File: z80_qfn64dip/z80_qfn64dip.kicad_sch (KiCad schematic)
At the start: 58 parts, among them J1 Conn_08, U1 Caravel_QFN, U2 Z80CPU, U3 TPS7A2033PDQNRM3, U4 TPS7A2018PDQNRM3, U5 TPS7A2050PDQNRM3, U6 AT25EU0081A, X1 10MHz

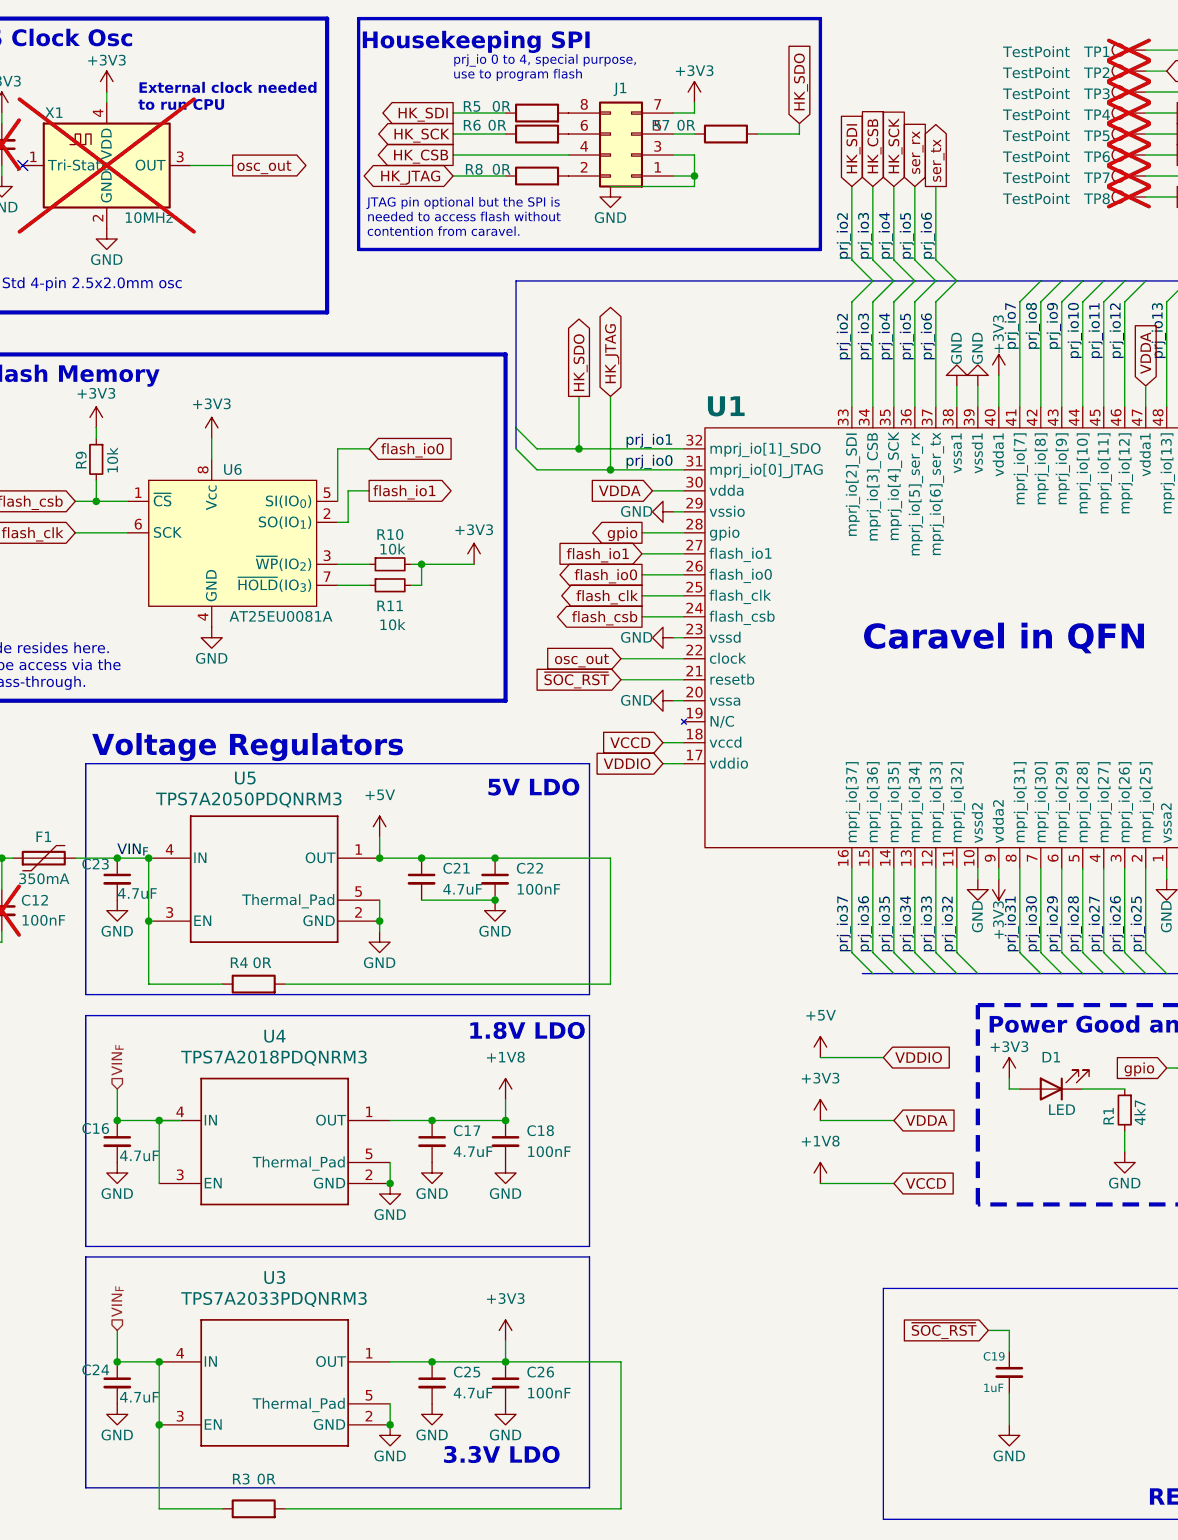
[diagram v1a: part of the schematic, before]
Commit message: remove signals from power layer moving them to bottom layer; change power routing from tracks to planes if they can be called as such
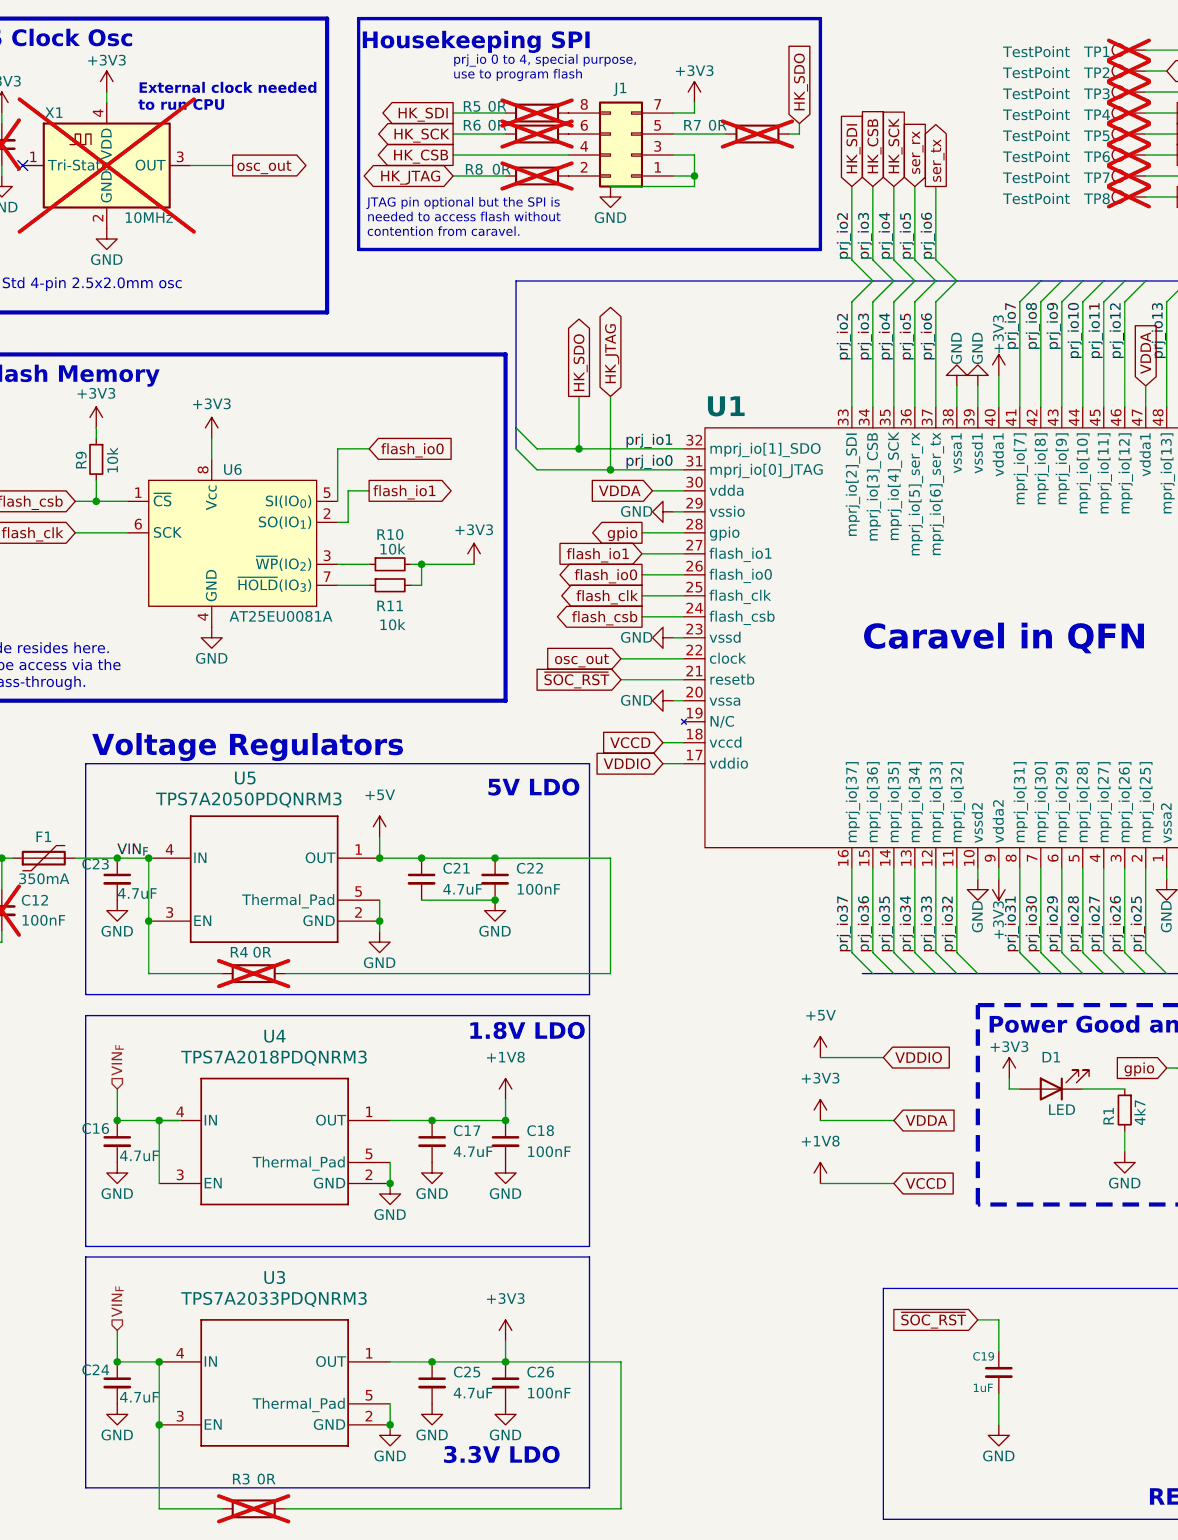
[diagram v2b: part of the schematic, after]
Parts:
- R3, R4, R5, R6, R7, R8: now not fitted
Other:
- moved on the sheet: C19
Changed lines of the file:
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@@
 	(wire
 		(pts
-			(xy 43.18 130.81) (xy 52.07 130.81)
+			(xy 43.18 129.54) (xy 52.07 129.54)
 		)
 		(stroke
@@
 	(wire
 		(pts
-			(xy 109.22 27.94) (xy 106.68 27.94)
+			(xy 113.03 27.94) (xy 106.68 27.94)
 		)
 		(stroke
@@
 	(wire
 		(pts
-			(xy 99.06 130.81) (xy 99.06 115.57)
+			(xy 99.06 129.54) (xy 99.06 115.57)
 		)
 		(stroke
@@
 	(wire
 		(pts
-			(xy 147.32 172.72) (xy 147.32 175.26)
+			(xy 146.05 171.45) (xy 146.05 175.26)
 		)
 		(stroke
@@
 	(wire
 		(pts
-			(xy 144.78 172.72) (xy 147.32 172.72)
+			(xy 143.51 171.45) (xy 146.05 171.45)
 		)
 		(stroke
@@
 	(wire
 		(pts
-			(xy 43.18 123.19) (xy 43.18 130.81)
+			(xy 43.18 123.19) (xy 43.18 129.54)
 		)
 		(stroke
@@
 	(wire
 		(pts
-			(xy 121.92 27.94) (xy 116.84 27.94)
+			(xy 121.92 27.94) (xy 120.65 27.94)
 		)
 		(stroke
@@
 	(wire
 		(pts
-			(xy 59.69 130.81) (xy 99.06 130.81)
+			(xy 59.69 129.54) (xy 99.06 129.54)
 		)
 		(stroke
@@
 	(wire
 		(pts
-			(xy 147.32 180.34) (xy 147.32 184.15)
+			(xy 146.05 180.34) (xy 146.05 184.15)
 		)
 		(stroke
@@
 			"TQEAAAA4BAAAZAEAAAAAAAAAAAAAWxMAAGcBAACIOadNAQAAADcEAABrAQAAAAAAAAAAAABbEwAA"
 			"bwEAAKg5p00BAAAANgQAAHMBAAAAAAAAAAAAAFsTAAB3AQAAyDmnTQEAAAAqBAAAewEAAAAAAAAA"
-			"AAAAWxMAAH4BAADoOadNAQAAACQEAACCAQAAAAAAAA=="
+			"AAAAWxMAAH4BAADoOadNAQAAACQEAACCAQAAAAAAAAEAAAAwTjsZAQAAABDeCg0BAAAAEA5qJgEA"
+			"AADwYFAmAQAAAIBaCw0BAAAA8KdpJgEAAAAwmmkmAQAAAEBbCw0BAAAAMJppJgEAAAAwmmkmAQAA"
+			"ADCaaSYBAAAAUI3/DAEAAAAwTjsZAQAAADBOOxkBAAAAME47GQEAAADwYFAmAQAAADCaaSYBAAAA"
+			"ME47GQEAAAAwqGkmAQAAAICaaSYBAAAA0N4KDQEAAACAmmkmAQAAAICaaSYBAAAAQA5qJgEAAAAw"
+			"TjsZAQAAABDeCg0BAAAAcA5qJgEAAADwYFAmAQAAAIBaCw0BAAAAcKhpJgEAAADQmmkmAQAAAEBb"
+			"Cw0BAAAA0JppJgEAAADQmmkmAQAAANCaaSYBAAAAUI3/DAEAAAAwTjsZAQAAADBOOxkBAAAAME47"
+			"GQEAAADwYFAmAQAAANCaaSYBAAAAME47GQEAAACgDmomAQAAALCoaSYBAAAA0N4KDQEAAACwqGkm"
+			"AQAAALCoaSYBAAAA0A5qJgEAAAAwTjsZAQAAABDeCg0BAAAAAA9qJgEAAACwSvkiAQAAAIBaCw0B"
+			"AAAAMA9qJgEAAADwqGkmAQAAAOBaCw0BAAAA8KhpJgEAAADwqGkmAQAAAPCoaSYBAAAAMKlpJgEA"
+			"AABAWwsNAQAAACCbaSYBAAAAUI3/DAEAAAAwTjsZAQAAADBOOxkBAAAAME47GQEAAACwSvkiAQAA"
+			"APCoaSYBAAAAME47GQEAAABwqWkmAQAAAHCbaSYBAAAA0N4KDQEAAABwm2kmAQAAAHCbaSYBAAAA"
+			"YA9qJgEAAAAwTjsZAQAAABDeCg0BAAAAkA9qJgEAAADwYFAmAQAAAIBaCw0BAAAAwJtpJgEAAABQ"
+			"11gmAQAAAOBaCw0BAAAAUNdYJgEAAABQ11gmAQAAAFDXWCYBAAAAkFYGDQEAAAAw6ZUJAQAAAEBb"
+			"Cw0BAAAAMOmVCQEAAABQjf8MAQAAADBOOxkBAAAAME47GQEAAAAwTjsZAQAAAPBgUCYBAAAAUNdY"
+			"JgEAAAAwTjsZAQAAALCpaSYBAAAAEJxpJgEAAADQ3goNAQAAABCcaSYBAAAAEJxpJgEAAADAD2om"
+			"AQAAADBOOxkBAAAAEN4KDQEAAAAwEGomAQAAAPBgUCYBAAAAgFoLDQEAAADwqWkmAQAAAGCcaSYB"
+			"AAAA4FoLDQEAAABgnGkmAQAAAGCcaSYBAAAAYJxpJgEAAACQVgYNAQAAADDplQkBAAAAQFsLDQEA"
+			"AAAw6ZUJAQAAAFCN/wwBAAAAME47GQEAAAAwTjsZAQAAAACMiCYBAAAA8A6IJgEAAAAAAAAAAAAA"
+			"AOEQAAAAAAAAAwAAAIapfiG6H/CUV+EGQSCGGQAAAA=="
 		)
 	)
@@
 	(global_label "~{SOC_RST}"
 		(shape input)
-		(at 144.78 172.72 180)
+		(at 143.51 171.45 180)
 		(fields_autoplaced yes)
 		(effects
@@
 		)
 		(property "Intersheetrefs" "${INTERSHEET_REFS}"
-			(at 133.5701 172.72 0)
+			(at 132.3001 171.45 0)
 			(effects
 				(font
@@
 		(lib_name "GND_2")
 		(lib_id "power:GND")
-		(at 147.32 184.15 0)
+		(at 146.05 184.15 0)
 		(unit 1)
 		(exclude_from_sim no)
@@
 		(dnp no)
 		(property "Reference" "#PWR044"
-			(at 147.32 190.5 0)
+			(at 146.05 190.5 0)
 			(effects
 				(font
@@
 		)
 		(property "Value" "GND"
-			(at 147.32 187.96 0)
+			(at 146.05 187.96 0)
 			(effects
 				(font
@@
 		)
 		(property "Footprint" ""
-			(at 147.32 184.15 0)
+			(at 146.05 184.15 0)
 			(effects
 				(font
@@
 		)
 		(property "Datasheet" ""
-			(at 147.32 184.15 0)
+			(at 146.05 184.15 0)
 			(effects
 				(font
@@
 		)
 		(property "Description" ""
-			(at 147.32 184.15 0)
+			(at 146.05 184.15 0)
 			(effects
 				(font
@@
 	(symbol
 		(lib_id "Device:R")
-		(at 55.88 130.81 90)
+		(at 55.88 129.54 90)
 		(unit 1)
 		(exclude_from_sim no)
 		(in_bom yes)
 		(on_board yes)
-		(dnp no)
+		(dnp yes)
 		(property "Reference" "R4"
-			(at 54.102 128.27 90)
+			(at 54.102 127 90)
 			(effects
 				(font
@@
 		)
 		(property "Value" "0R"
-			(at 56.896 128.27 90)
+			(at 56.896 127 90)
 			(effects
 				(font
@@
 		)
 		(property "Footprint" "Resistor_SMD:R_0402_1005Metric_Pad0.72x0.64mm_HandSolder"
-			(at 55.88 132.588 90)
+			(at 55.88 131.318 90)
 			(effects
 				(font
@@
 		)
 		(property "Datasheet" "~"
-			(at 55.88 130.81 0)
+			(at 55.88 129.54 0)
 			(effects
 				(font
@@
 		)
 		(property "Description" "Resistor"
-			(at 55.88 130.81 0)
+			(at 55.88 129.54 0)
 			(effects
 				(font
@@
 		(in_bom yes)
 		(on_board yes)
-		(dnp no)
+		(dnp yes)
 		(property "Reference" "R3"
 			(at 54.356 190.754 90)
@@
 	(symbol
 		(lib_id "Device:R")
-		(at 113.03 27.94 90)
+		(at 116.84 27.94 90)
 		(unit 1)
 		(exclude_from_sim no)
 		(in_bom yes)
 		(on_board yes)
-		(dnp no)
+		(dnp yes)
 		(property "Reference" "R7"
-			(at 105.156 26.924 90)
+			(at 108.966 26.924 90)
 			(effects
 				(font
@@
 		)
 		(property "Value" "0R"
-			(at 108.204 26.924 90)
+			(at 112.014 26.924 90)
 			(effects
 				(font
@@
 		)
 		(property "Footprint" "Resistor_SMD:R_0402_1005Metric_Pad0.72x0.64mm_HandSolder"
-			(at 113.03 29.718 90)
+			(at 116.84 29.718 90)
 			(effects
 				(font
@@
 		)
 		(property "Datasheet" "~"
-			(at 113.03 27.94 0)
+			(at 116.84 27.94 0)
 			(effects
 				(font
@@
 		)
 		(property "Description" "Resistor"
-			(at 113.03 27.94 0)
+			(at 116.84 27.94 0)
 			(effects
 				(font
@@
 		(in_bom yes)
 		(on_board yes)
-		(dnp no)
+		(dnp yes)
 		(property "Reference" "R5"
 			(at 82.296 24.638 90)
@@
 		)
 		(property "Value" "0R"
-			(at 85.852 24.638 90)
+			(at 85.344 24.638 90)
 			(effects
 				(font
@@
 	(symbol
 		(lib_id "Device:C_Small")
-		(at 147.32 177.8 0)
+		(at 146.05 177.8 0)
 		(unit 1)
 		(exclude_from_sim no)
@@
 		(dnp no)
 		(property "Reference" "C19"
-			(at 144.145 175.895 0)
+			(at 142.875 175.895 0)
 			(effects
 				(font
@@
 		)
 		(property "Value" "1uF"
-			(at 144.145 179.705 0)
+			(at 142.875 179.705 0)
 			(effects
 				(font
@@
 		)
 		(property "Footprint" "Capacitor_SMD:C_0402_1005Metric"
-			(at 147.32 177.8 0)
+			(at 146.05 177.8 0)
 			(effects
 				(font
@@
 		)
 		(property "Datasheet" "~"
-			(at 147.32 177.8 0)
+			(at 146.05 177.8 0)
 			(effects
 				(font
@@
 		)
 		(property "Description" ""
-			(at 147.32 177.8 0)
+			(at 146.05 177.8 0)
 			(effects
 				(font
@@
 		)
 		(property "JLC" ""
-			(at 147.32 177.8 0)
+			(at 146.05 177.8 0)
 			(effects
 				(font
@@
 		)
 		(property "Part number" ""
-			(at 147.32 177.8 0)
+			(at 146.05 177.8 0)
 			(effects
 				(font
@@
 		)
 		(property "MPN" ""
-			(at 147.32 177.8 0)
+			(at 146.05 177.8 0)
 			(effects
 				(font
@@
 		(in_bom yes)
 		(on_board yes)
-		(dnp no)
+		(dnp yes)
 		(property "Reference" "R6"
 			(at 82.296 26.924 90)
@@
 		(in_bom yes)
 		(on_board yes)
-		(dnp no)
+		(dnp yes)
 		(property "Reference" "R8"
 			(at 82.55 32.258 90)

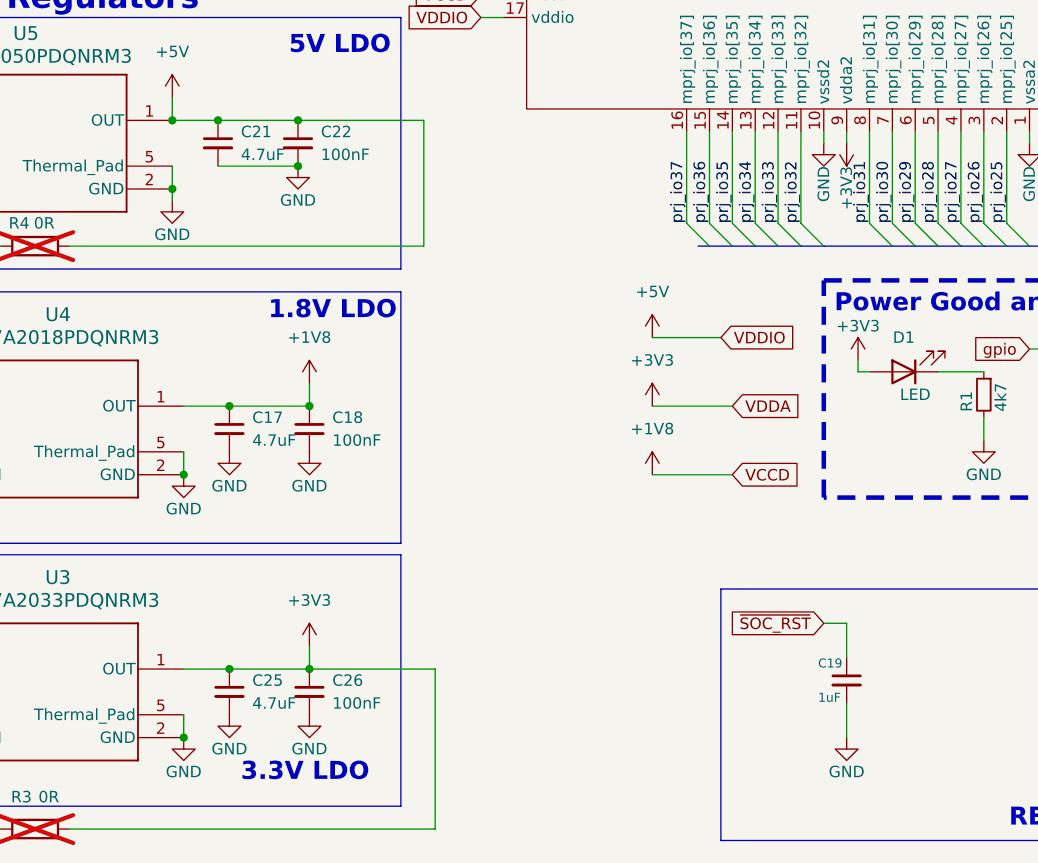
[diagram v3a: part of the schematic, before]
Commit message: mainly layout changes, remove kicad_prl from comitted files
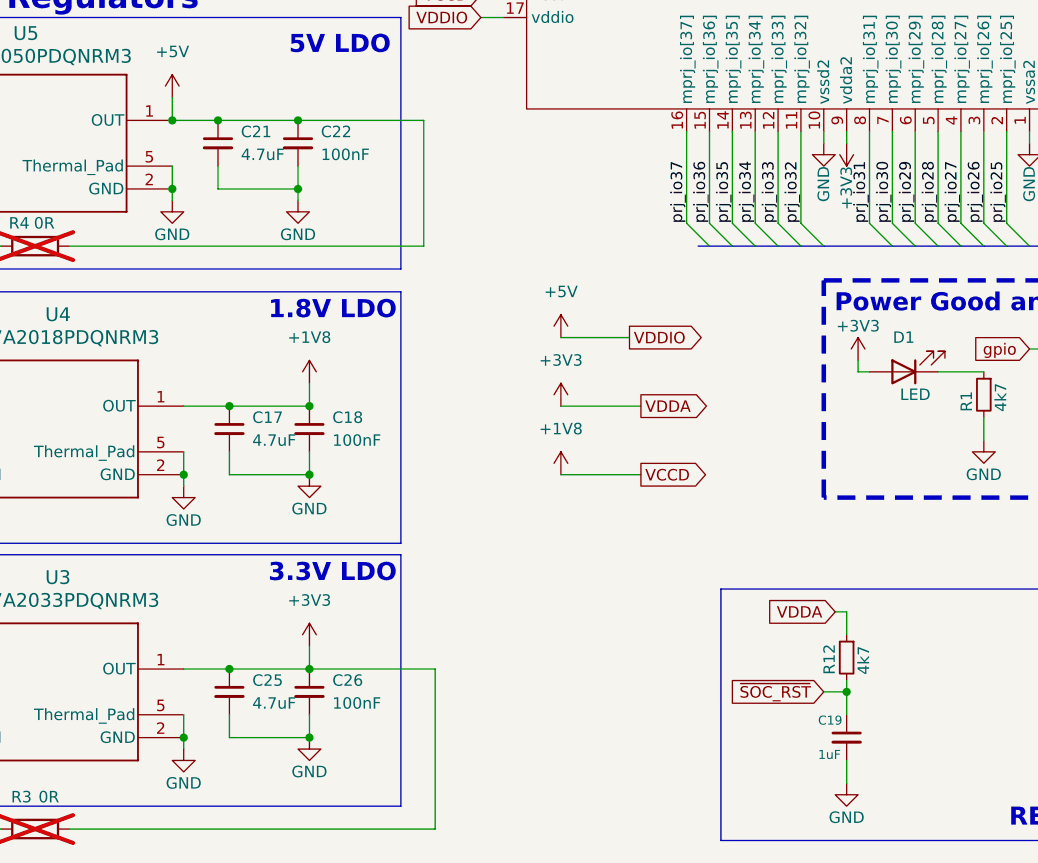
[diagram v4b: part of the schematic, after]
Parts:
- added R12: 4k7, Resistor_SMD:R_0402_1005Metric, symbol Device:R_Small
- C6, C7: footprint Capacitor_SMD:C_0603_1608Metric_Pad1.08x0.95mm_HandSolder -> Capacitor_SMD:C_0402_1005Metric
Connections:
- net +3V3: now also R12.1
- net ~{SOC_RST}: now also R12.2
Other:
- moved on the sheet: C19

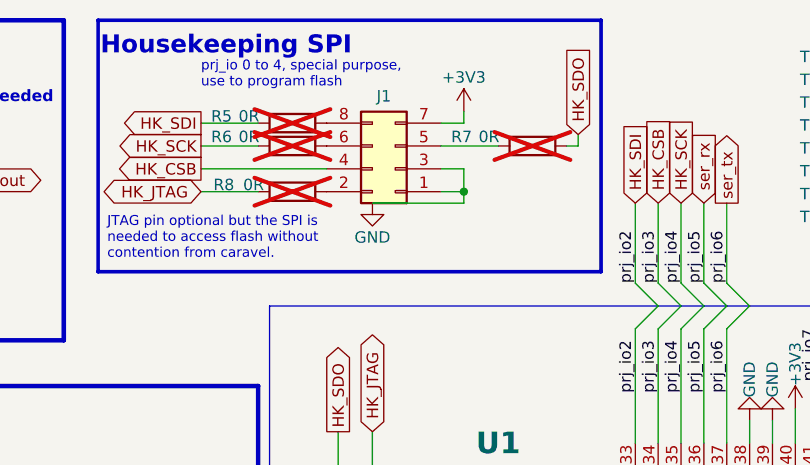
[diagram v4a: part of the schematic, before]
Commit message: move everything to front side; label pins
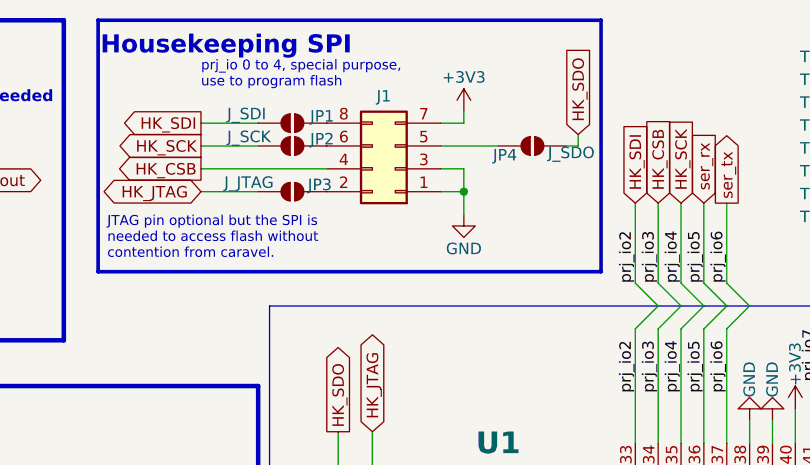
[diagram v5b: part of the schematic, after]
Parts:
- removed R5, R6, R7, R8: 0R, Resistor_SMD:R_0402_1005Metric_Pad0.72x0.64mm_HandSolder, symbol Device:R
- added JP1: J_SDI, ProjectLibrary:SolderJumper-2_P2x0.9mm_Open_TrianglePad, symbol Jumper:SolderJumper_2_Open
- added JP2: J_SCK, ProjectLibrary:SolderJumper-2_P2x0.9mm_Open_TrianglePad, symbol Jumper:SolderJumper_2_Open
- added JP3: J_JTAG, ProjectLibrary:SolderJumper-2_P2x0.9mm_Open_TrianglePad, symbol Jumper:SolderJumper_2_Open
- added JP4: J_SDO, ProjectLibrary:SolderJumper-2_P2x0.9mm_Open_TrianglePad, symbol Jumper:SolderJumper_2_Open
- C10, C5, C8, C9: footprint Capacitor_SMD:C_0603_1608Metric_Pad1.08x0.95mm_HandSolder -> Capacitor_SMD:C_0402_1005Metric
- C2, C4: footprint Capacitor_SMD:C_0402_1005Metric_Pad0.74x0.62mm_HandSolder -> Capacitor_SMD:C_0402_1005Metric
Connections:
- net HK_JTAG: now also JP3.1 (A)
- net HK_SCK: now also JP2.1 (A)
- net HK_SDI: now also JP1.1 (A)
- net HK_SDO: now also JP4.1 (A)
- net at J1.5 (Pin_5): now also JP4.2 (B)
- net at J1.8 (Pin_8): now also JP1.2 (B)
- net at J1.2 (Pin_2): now also JP3.2 (B)
- net at J1.6 (Pin_6): now also JP2.2 (B)
